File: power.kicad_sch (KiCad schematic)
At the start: 13 parts, among them U4 AMS1117-3.3

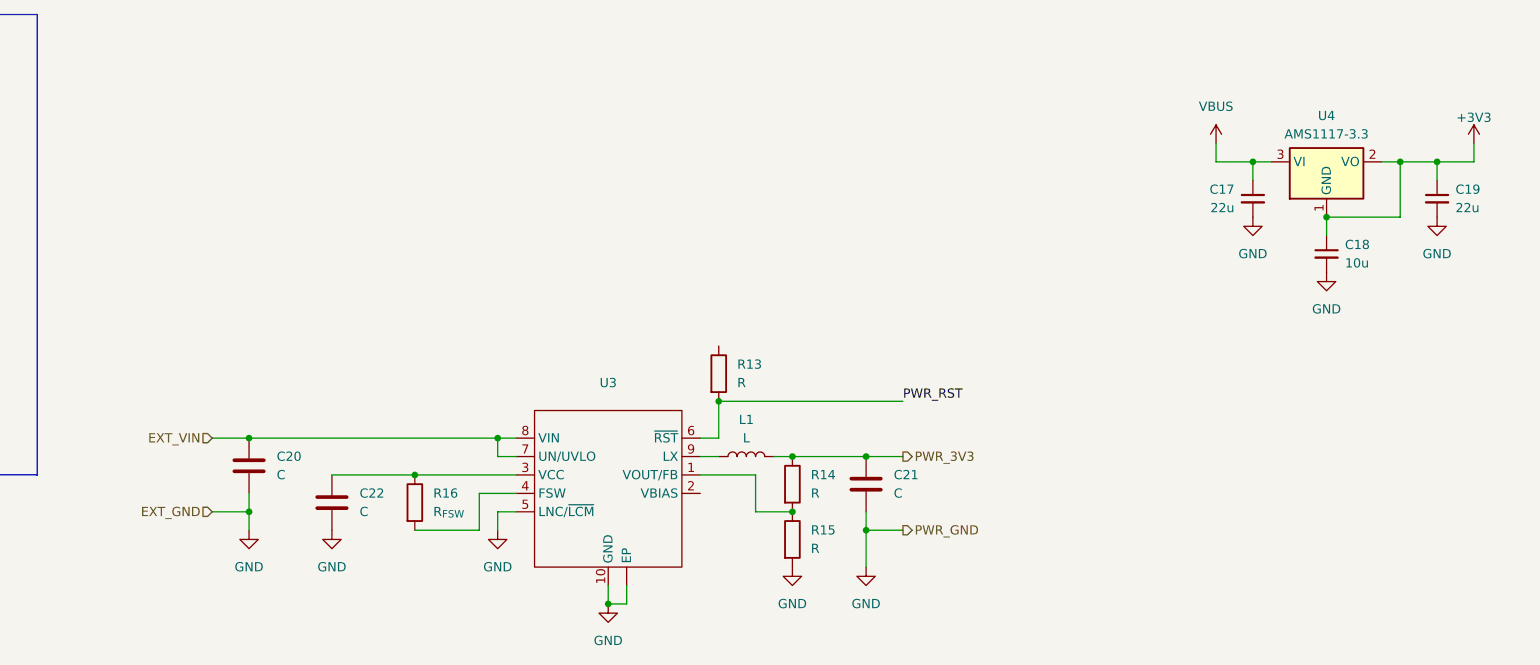
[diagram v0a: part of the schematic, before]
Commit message: Block diagram
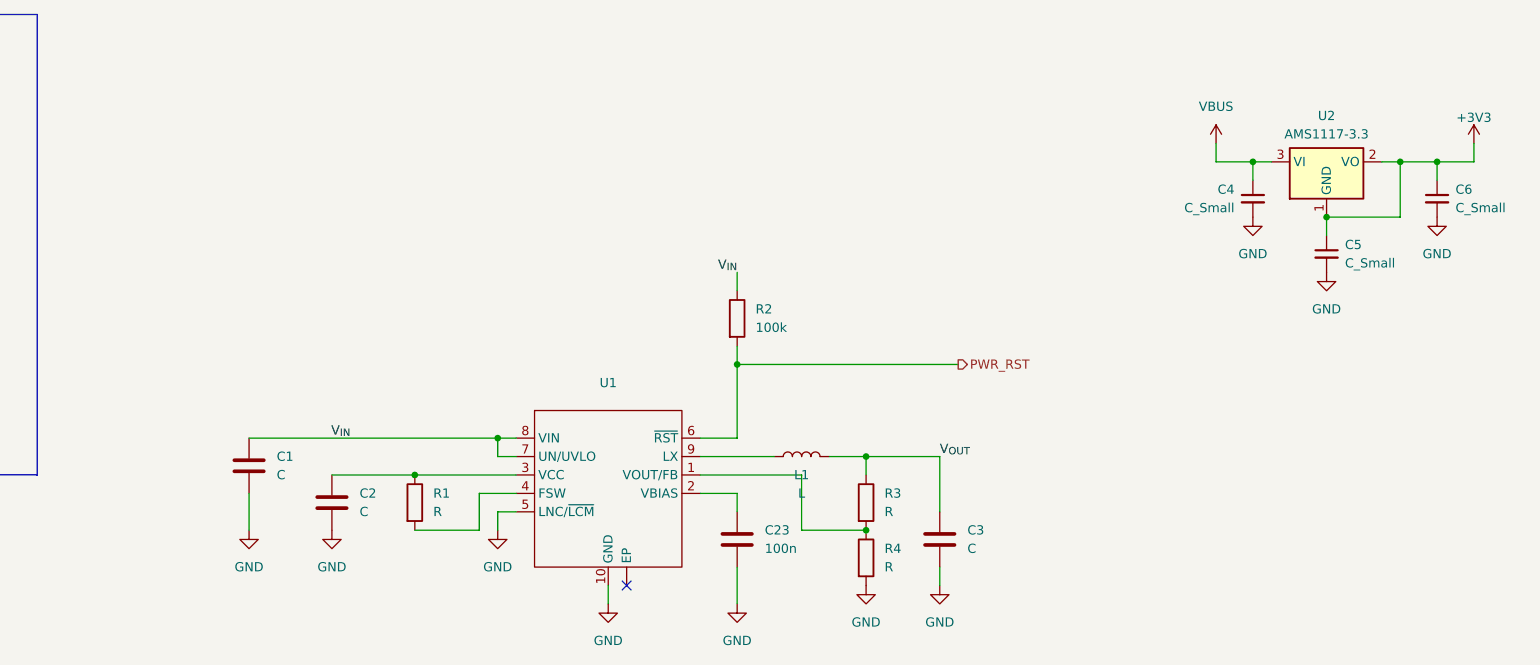
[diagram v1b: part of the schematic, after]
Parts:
- added C23: 100n, Capacitor_SMD:C_0402_1005Metric, symbol Device:C
- C1: renamed from C20; footprint (none) -> Capacitor_SMD:C_0402_1005Metric
- C2: renamed from C22; footprint (none) -> Capacitor_SMD:C_0402_1005Metric
- C3: renamed from C21; footprint (none) -> Capacitor_SMD:C_0402_1005Metric
- C4: renamed from C17; value 22u -> C_Small; footprint Capacitor_SMD:C_1206_3216Metric -> Capacitor_SMD:C_0402_1005Metric
- C5: renamed from C18; value 10u -> C_Small; footprint Capacitor_SMD:C_1206_3216Metric -> Capacitor_SMD:C_0402_1005Metric
- C6: renamed from C19; value 22u -> C_Small; footprint Capacitor_SMD:C_1206_3216Metric -> Capacitor_SMD:C_0402_1005Metric
- R1: renamed from R16; value R_{FSW} -> R; footprint (none) -> Resistor_SMD:R_0402_1005Metric
- R2: renamed from R13; value R -> 100k; footprint (none) -> Resistor_SMD:R_0402_1005Metric
- R3: renamed from R14; footprint (none) -> Resistor_SMD:R_0402_1005Metric
- R4: renamed from R15; footprint (none) -> Resistor_SMD:R_0402_1005Metric
- U1: renamed from U3; footprint cubesat_rp2040:DFN-10-1EP_3x3mm_P0.5mm_EP0.98x0.62mm_Offset0.15mm -> (none)
- U2: renamed from U4; footprint Package_TO_SOT_SMD:SOT-223-3_TabPin2 -> (none)
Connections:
- net EXT_VIN is gone; now on net V_{IN}: C1.1, U1.7 (UN/UVLO), U1.8 (VIN)
- net GND: now also C23.2; no longer U1. (EP)
- net at U1.2 (VBIAS): now also C23.1
- net V_{IN}: now reaches R2.1
- net PWR_3V3 renamed V_{OUT}
- no-connect marks 0 -> 1
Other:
- moved on the sheet: C3, L1, R2, R3, R4

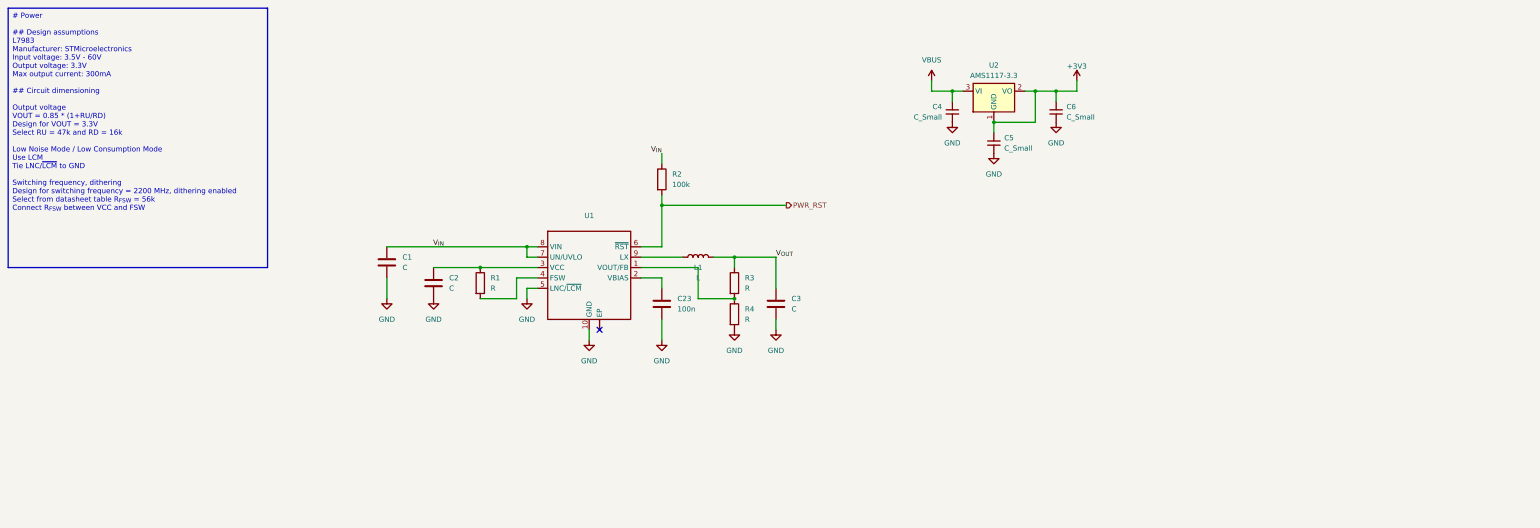
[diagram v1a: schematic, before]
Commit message: Complete power regulator schematics
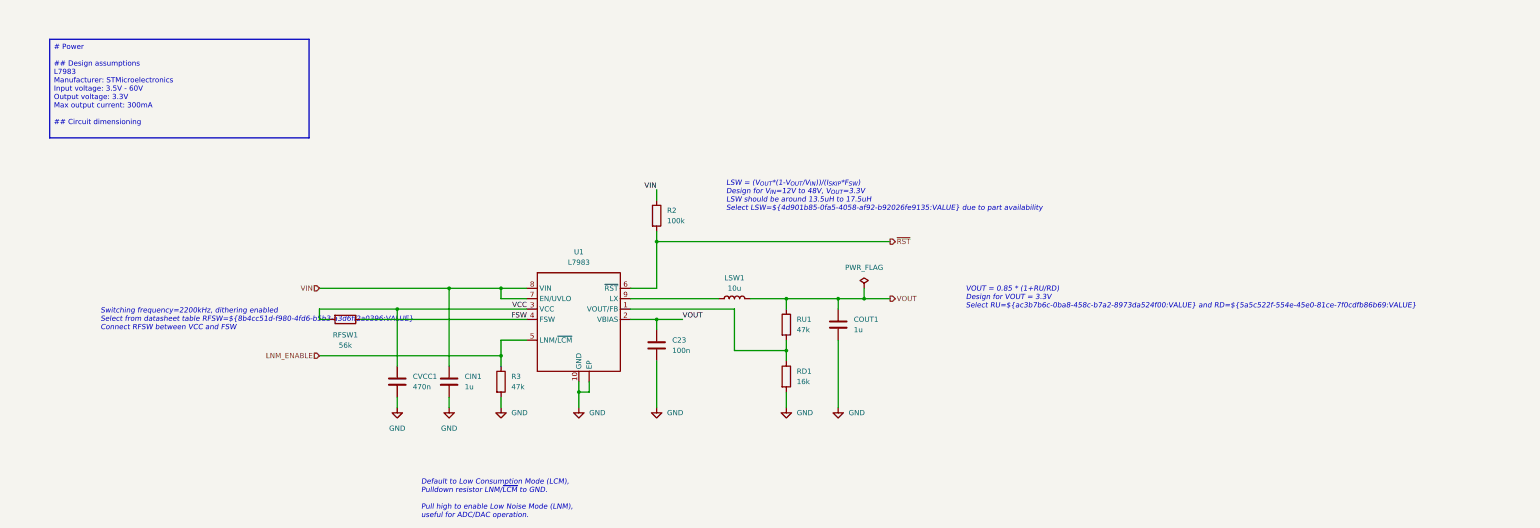
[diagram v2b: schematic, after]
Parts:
- removed C1, C2: C, Capacitor_SMD:C_0402_1005Metric, symbol Device:C
- removed C4, C5, C6: C_Small, Capacitor_SMD:C_0402_1005Metric, symbol Device:C_Small
- removed R1: R, Resistor_SMD:R_0402_1005Metric, symbol Device:R
- removed U2: AMS1117-3.3, symbol Regulator_Linear:AMS1117-3.3
- added CIN1: 1u, Capacitor_SMD:C_0402_1005Metric, symbol Device:C
- added CVCC1: 470n, Capacitor_SMD:C_0402_1005Metric, symbol Device:C
- added R3: 47k, Resistor_SMD:R_0402_1005Metric, symbol Device:R
- added RFSW1: 56k, Resistor_SMD:R_0402_1005Metric, symbol Device:R
- COUT1: renamed from C3; value C -> 1u
- LSW1: renamed from L1; value L -> 10u; footprint (none) -> Resistor_SMD:R_0402_1005Metric
- RD1: renamed from R4; value R -> 16k
- RU1: renamed from R3; value R -> 47k
- U1: value ~ -> L7983; footprint (none) -> cubesat_rp2040:DFN-10-1EP_3x3mm_P0.5mm_EP0.62x0.98mm_Offset0.15mm
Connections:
- net V_{OUT} is gone; now on net VOUT: COUT1.1, LSW1.2, RU1.1
- net GND: now also U1. (EP), CIN1.2, CVCC1.2, R3.2; no longer U1.5 (LNC/~{LCM})
- net VOUT: now reaches C23.1, U1.2 (VBIAS)
- net VCC: now reaches U1.3 (VCC)
- net VCC: now also CVCC1.1, RFSW1.2
- net FSW: now reaches U1.4 (FSW)
- net FSW: now also RFSW1.1
- net PWR_RST renamed ~{RST}
- net V_{IN} renamed VIN
- net VIN: now also CIN1.1
- new net LNM_ENABLE: R3.1, U1.5 (LNM/~{LCM})
- no-connect marks 1 -> 0
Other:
- note added: "Default to Low Consumption Mode (LCM), Pulldown resistor LNM/~{LCM} to GND. Pull high to enable Low Noise Mode (LNM), useful for ADC/DAC operation."
- note added: "LSW = (V_{OUT}*(1-V_{OUT}/V_{IN}))/(I_{SKIP}*F_{SW}) Design for V_{IN}=12V to 48V, V_{OUT}=3.3V LSW should be around 13.5uH to 17.5uH Select LSW=${4d901b85-0fa5-4058-af92-b92026fe9135:VALUE} due to part availability"
- note added: "Switching frequency=2200kHz, dithering enabled Select from datasheet table RFSW=${8b4cc51d-f980-4fd6-b5b3-a3d6ff2a0396:VALUE} Connect RFSW between VCC and FSW"
- note added: "VOUT = 0.85 * (1+RU/RD) Design for VOUT = 3.3V Select RU=${ac3b7b6c-0ba8-458c-b7a2-8973da524f00:VALUE} and RD=${5a5c522f-554e-45e0-81ce-7f0cdfb86b69:VALUE}"
- moved on the sheet: C23, COUT1, LSW1, R2, RD1, RU1, U1

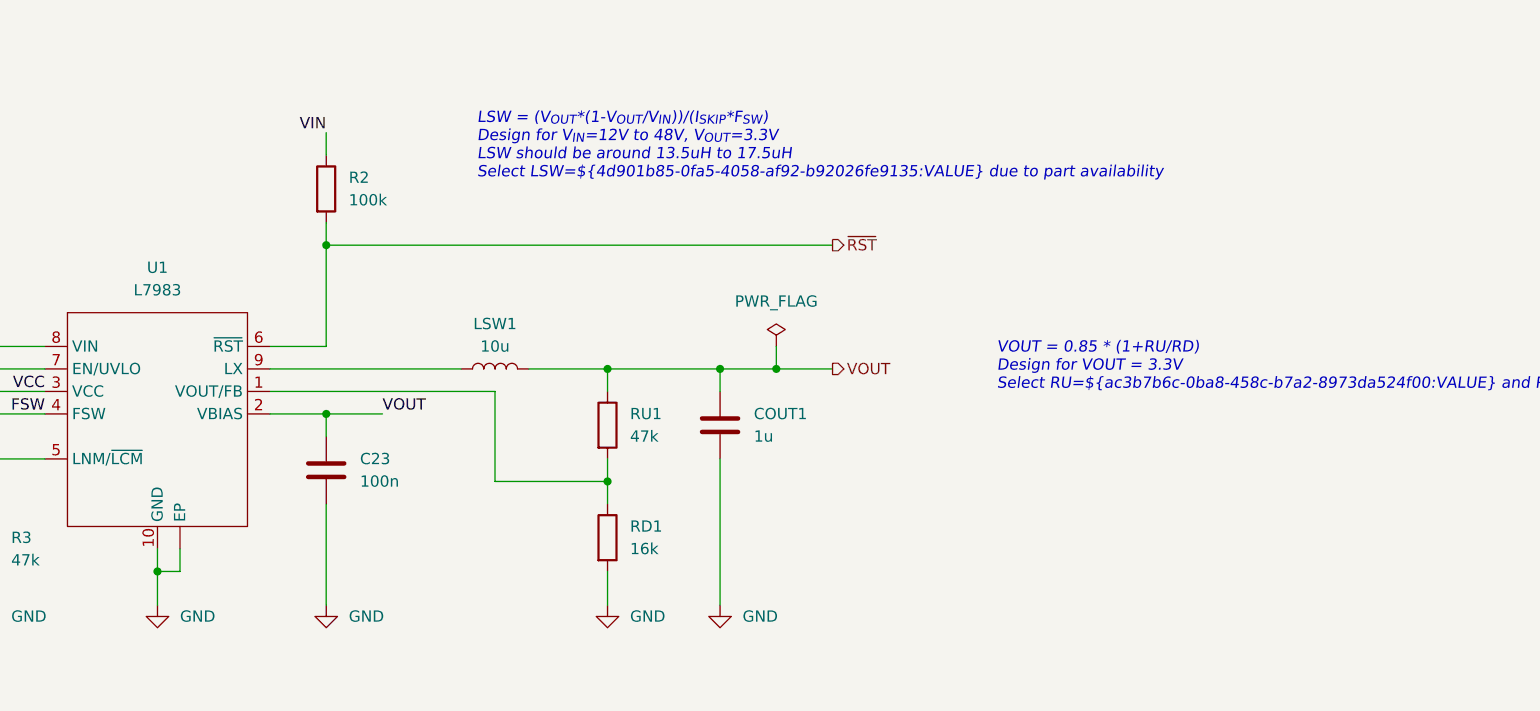
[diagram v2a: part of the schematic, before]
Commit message: Update footprints, route switching regulator circuit block
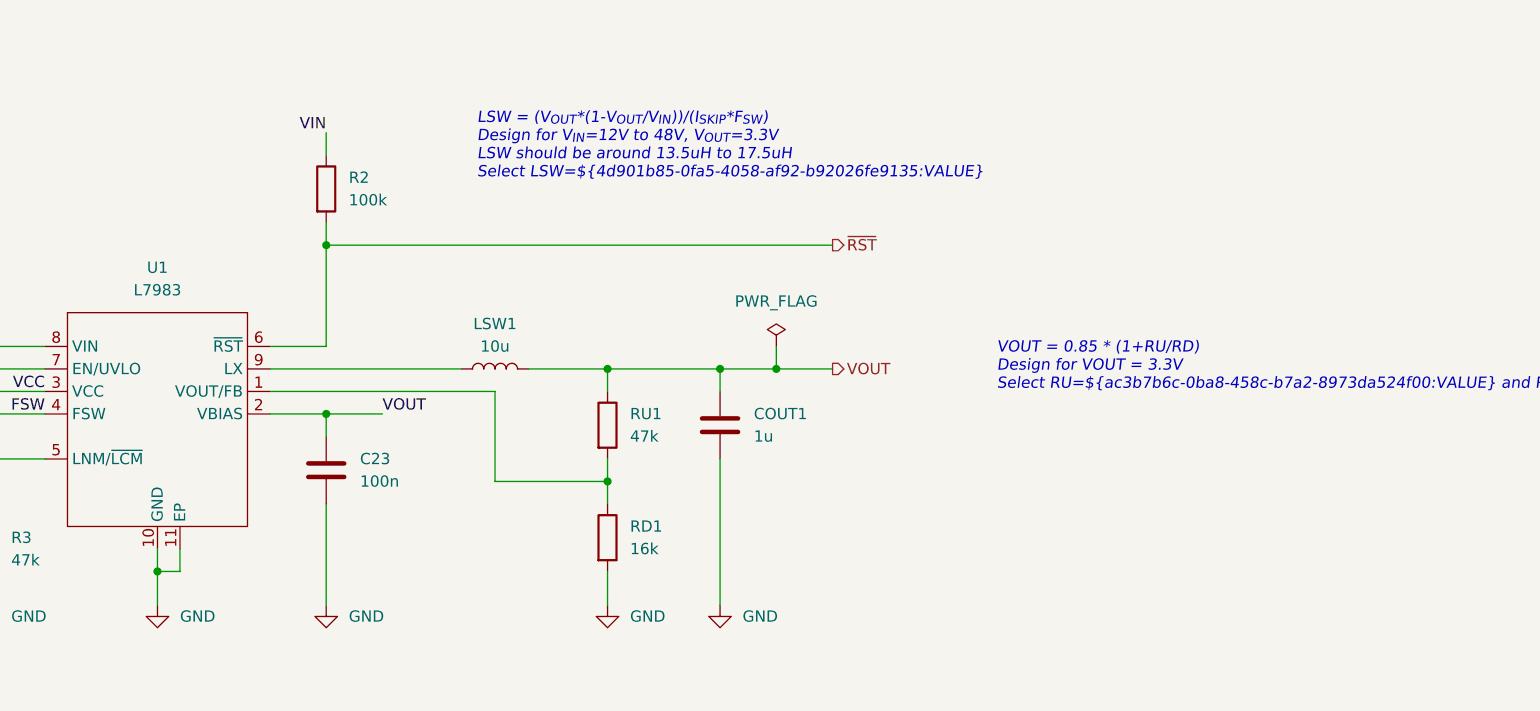
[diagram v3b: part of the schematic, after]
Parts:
- CIN1, COUT1: footprint Capacitor_SMD:C_0402_1005Metric -> Capacitor_SMD:C_0805_2012Metric
- LSW1: footprint Resistor_SMD:R_0402_1005Metric -> Inductor_SMD:L_1210_3225Metric
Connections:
- net GND: now also U1.11 (EP); no longer U1. (EP)
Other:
- note added: "LSW = (V_{OUT}*(1-V_{OUT}/V_{IN}))/(I_{SKIP}*F_{SW}) Design for V_{IN}=12V to 48V, V_{OUT}=3.3V LSW should be around 13.5uH to 17.5uH Select LSW=${4d901b85-0fa5-4058-af92-b92026fe9135:VALUE}"
- note removed: "LSW = (V_{OUT}*(1-V_{OUT}/V_{IN}))/(I_{SKIP}*F_{SW}) Design for V_{IN}=12V to 48V, V_{OUT}=3.3V LSW should be around 13.5uH to 17.5uH Select LSW=${4d901b85-0fa5-4058-af92-b92026fe9135:VALUE} due to part availability"
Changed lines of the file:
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@@
 		)
 	)
-	(text "LSW = (V_{OUT}*(1-V_{OUT}/V_{IN}))/(I_{SKIP}*F_{SW})\nDesign for V_{IN}=12V to 48V, V_{OUT}=3.3V\nLSW should be around 13.5uH to 17.5uH\nSelect LSW=${4d901b85-0fa5-4058-af92-b92026fe9135:VALUE} due to part availability"
+	(text "LSW = (V_{OUT}*(1-V_{OUT}/V_{IN}))/(I_{SKIP}*F_{SW})\nDesign for V_{IN}=12V to 48V, V_{OUT}=3.3V\nLSW should be around 13.5uH to 17.5uH\nSelect LSW=${4d901b85-0fa5-4058-af92-b92026fe9135:VALUE}"
 		(exclude_from_sim no)
 		(at 188.468 58.674 0)
@@
 		(pin "6"
 		)
-		(pin ""
+		(pin "11"
 		)
 		(pin "2"
@@
 			)
 		)
-		(property "Footprint" "Resistor_SMD:R_0402_1005Metric"
+		(property "Footprint" "Inductor_SMD:L_1210_3225Metric"
 			(at 190.5 83.82 0)
 			(effects
@@
 			)
 		)
-		(property "Footprint" "Capacitor_SMD:C_0402_1005Metric"
+		(property "Footprint" "Capacitor_SMD:C_0805_2012Metric"
 			(at 216.8652 93.98 0)
 			(effects
@@
 			)
 		)
-		(property "Footprint" "Capacitor_SMD:C_0402_1005Metric"
+		(property "Footprint" "Capacitor_SMD:C_0805_2012Metric"
 			(at 121.6152 107.95 0)
 			(effects
